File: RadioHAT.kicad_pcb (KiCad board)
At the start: 2 copper layers, 65 x 56.5 mm, 36 parts, among them J1 RPi_GPIO, J3 Conn_02x07_Odd_Even, J4 Conn_02x07_Odd_Even, U1 INA219AxD, U2 LP3855-ADJ

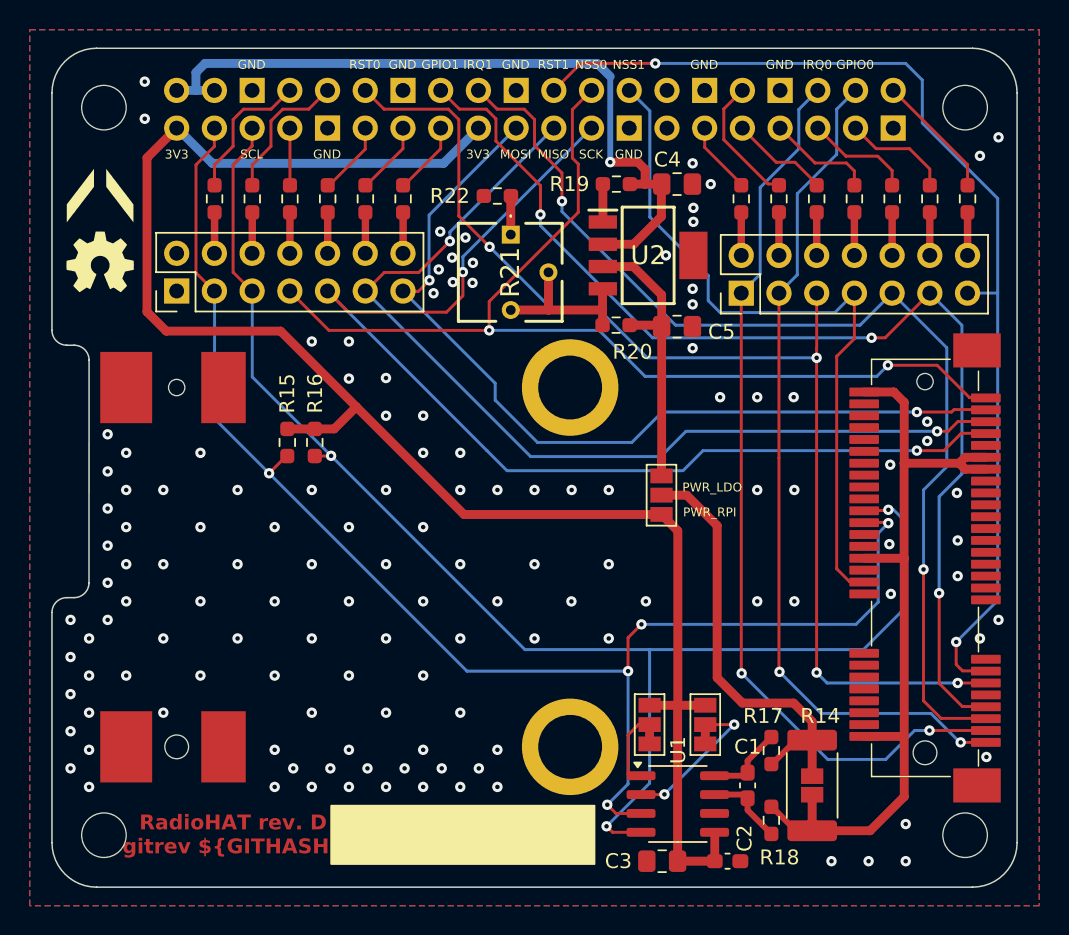
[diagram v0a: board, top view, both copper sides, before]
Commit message: Fix possible collision with supply voltage solder bridge
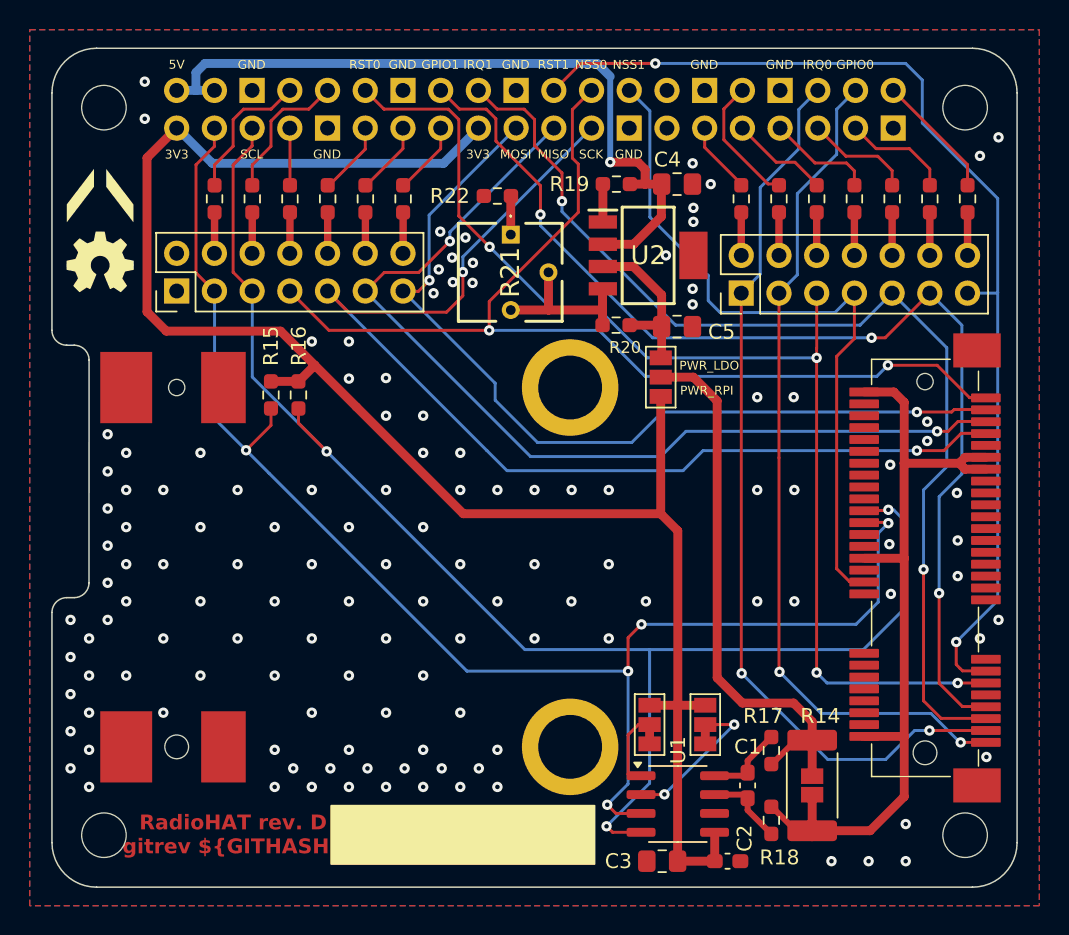
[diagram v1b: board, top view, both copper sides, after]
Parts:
- moved JP5 7.95 mm to (148.5, 92.4)
- moved R16 3.38 mm to (124.1, 93.6)
- moved R15 3.38 mm to (122.2, 93.6)
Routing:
- net Net-(JP5-C): track 27.1 -> 35.4 mm
- net Net-(JP5-A): track 19.2 -> 11.3 mm
- net +3.3V: track 113.1 -> 119.2 mm
- net SCL: track 96.2 -> 98.8 mm
- net SDA: track 96.6 -> 98.4 mm
- net GND: vias 132 -> 130
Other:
- board text added: "5V"

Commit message: Add 5V power channel for PCI cards
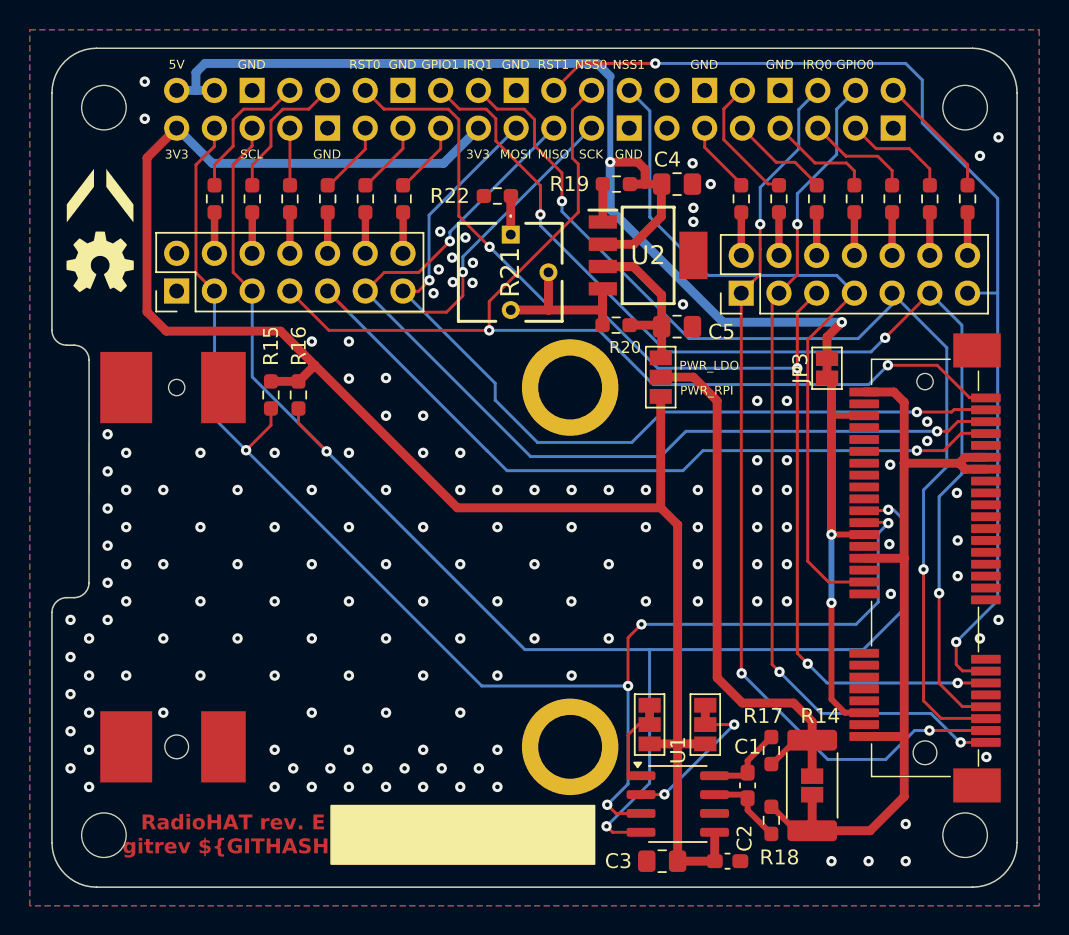
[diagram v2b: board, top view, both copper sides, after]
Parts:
- added JP3: SolderJumper_2_Bridged, Jumper:SolderJumper-2_P1.3mm_Bridged_Pad1.0x1.5mm, F.Cu at (159.7, 91.8)
- turned JP1 to -90 degrees
- turned JP2 to -90 degrees
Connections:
- J2 pad 28: unconnected-(J2-5V-Pad28) -> Net-(JP3-A)
- J2 pad 48: unconnected-(J2-5V-Pad48) -> Net-(JP3-A)
- J2 pad 6: unconnected-(J2-5V-Pad6) -> Net-(JP3-A)
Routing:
- net Net-(JP3-A): track 0.00 -> 28.8 mm, vias 0 -> 2
- net +5V: track 50.6 -> 75.4 mm, vias 1 -> 2
- net IRQ1: track 72.2 -> 73.4 mm
- net GPIO1: track 75.2 -> 76.0 mm
- net GPIO0: track 57.2 -> 57.6 mm, vias 2 -> 3
- net IRQ0: vias 2 -> 3
- net GND: vias 130 -> 146
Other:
- board text added: "RadioHAT rev. E gitrev ${GITHASH}"
- board text removed: "RadioHAT rev. D gitrev ${GITHASH}"
